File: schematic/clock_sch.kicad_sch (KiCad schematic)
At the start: 3 parts

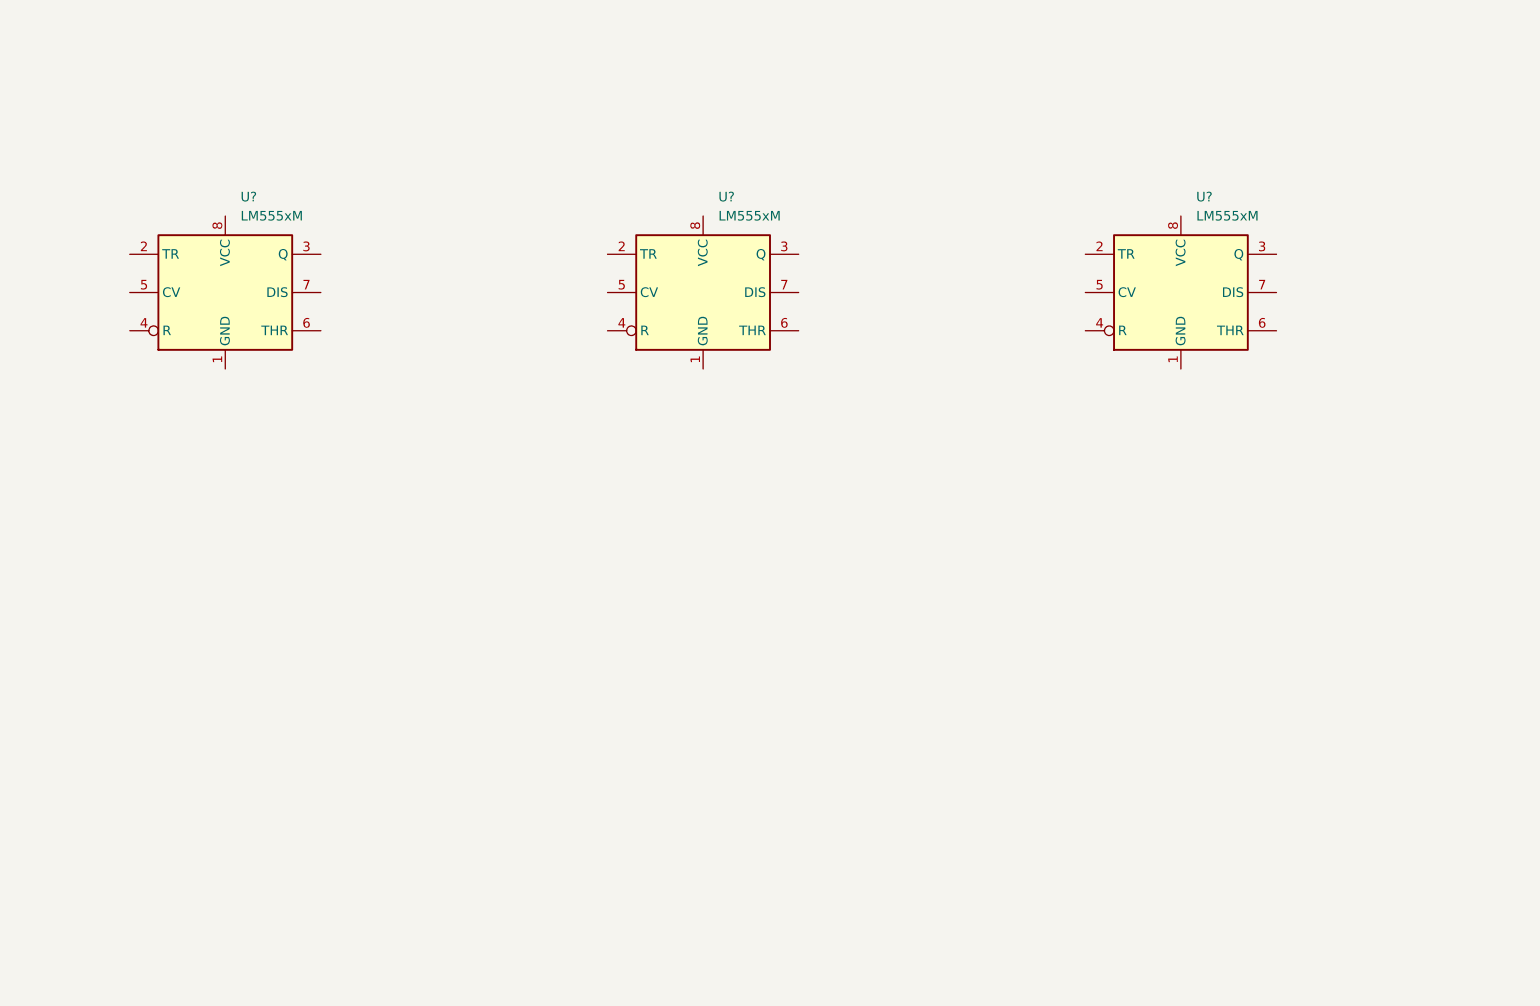
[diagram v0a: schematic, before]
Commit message: added astable clock schematic
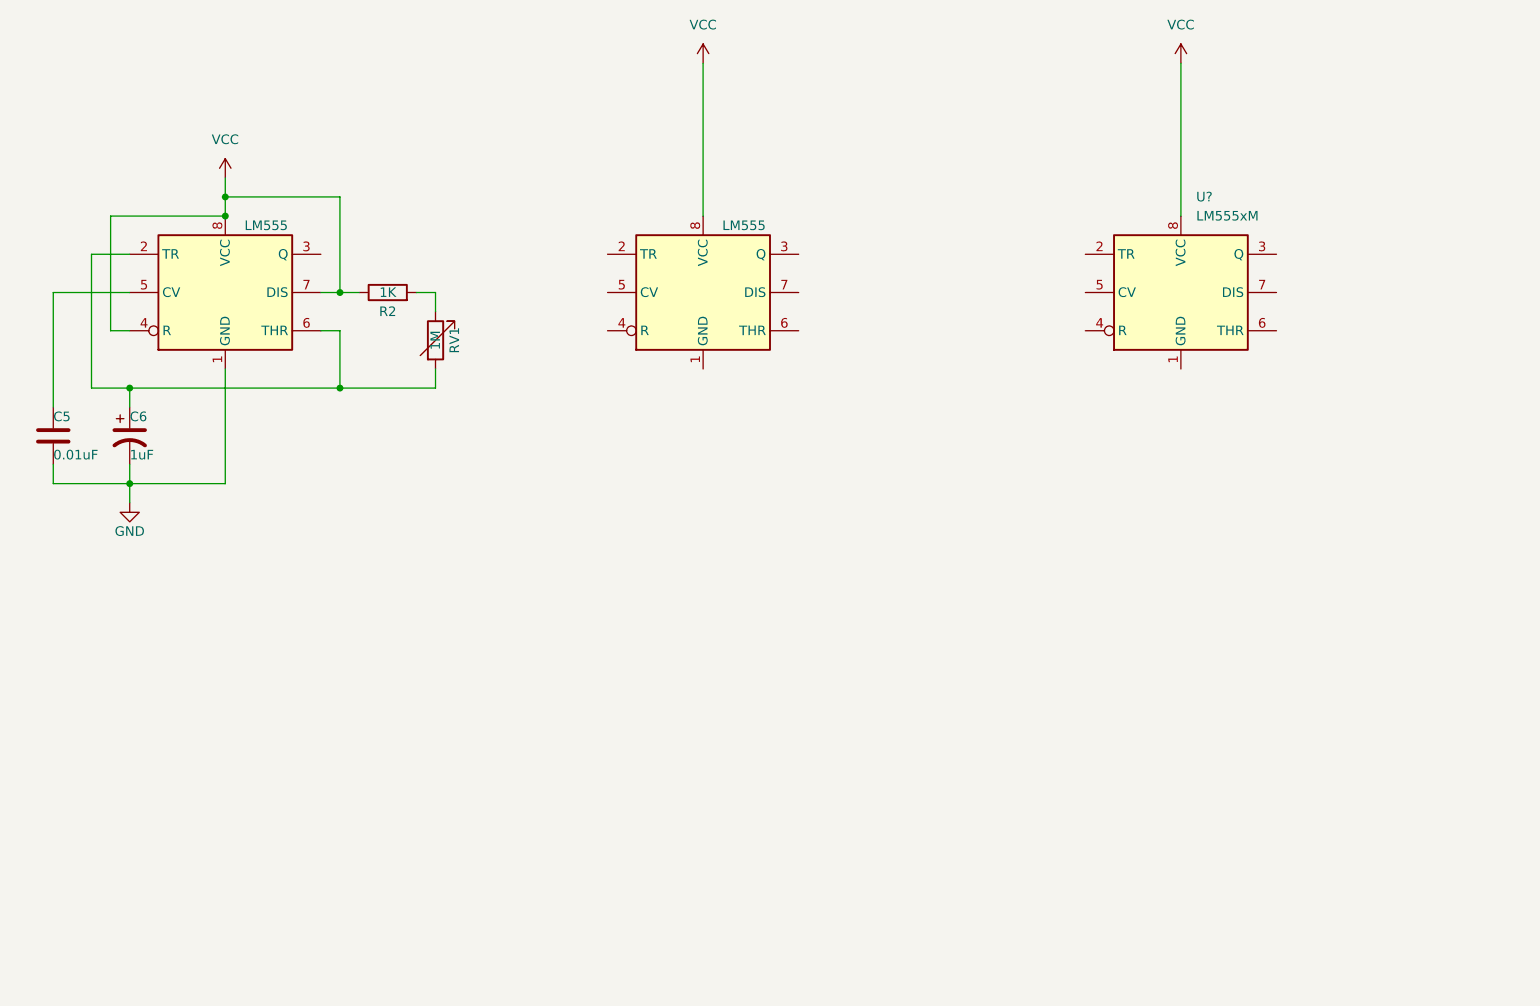
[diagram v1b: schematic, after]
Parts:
- added C5: 0.01uF, symbol Device:C
- added C6: 1uF, symbol Device:C_Polarized_US
- added R2: 1K, symbol Device:R
- added RV1: 1M, symbol Device:R_Variable
- U? (x2): value LM555xM -> LM555
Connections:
- net VCC: now reaches U?.8 (VCC)
- net VCC: now also U?.4 (R), U?.7 (DIS), U?.8 (VCC), U?.8 (VCC), R2.1
- net GND: now reaches U?.1 (GND)
- net GND: now also C5.2, C6.2
- net at U?.2 (TR): now also U?.6 (THR), C6.1, RV1.2
- net at U?.5 (CV): now also C5.1
- new net: R2.2, RV1.1
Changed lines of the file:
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@@
 (kicad_sch (version 20211123) (generator eeschema)
   (paper "A4")
+  (junction (at 63.5 60.96) (diameter 0) (color 0 0 0 0)
+  )
+  (junction (at 78.74 71.12) (diameter 0) (color 0 0 0 0)
+  )
+  (junction (at 63.5 58.42) (diameter 0) (color 0 0 0 0)
+  )
+  (junction (at 50.8 83.82) (diameter 0) (color 0 0 0 0)
+  )
+  (junction (at 78.74 83.82) (diameter 0) (color 0 0 0 0)
+  )
+  (junction (at 50.8 96.52) (diameter 0) (color 0 0 0 0)
+  )
+  (wire (pts (xy 63.5 60.96) (xy 48.26 60.96))
+    (stroke (width 0) (type default) (color 0 0 0 0))
+  )
+  (wire (pts (xy 63.5 55.88) (xy 63.5 58.42))
+    (stroke (width 0) (type default) (color 0 0 0 0))
+  )
+  (wire (pts (xy 91.44 81.28) (xy 91.44 83.82))
+    (stroke (width 0) (type default) (color 0 0 0 0))
+  )
+  (wire (pts (xy 190.5 40.64) (xy 190.5 60.96))
+    (stroke (width 0) (type default) (color 0 0 0 0))
+  )
+  (wire (pts (xy 78.74 58.42) (xy 78.74 71.12))
+    (stroke (width 0) (type default) (color 0 0 0 0))
+  )
+  (wire (pts (xy 78.74 83.82) (xy 91.44 83.82))
+    (stroke (width 0) (type default) (color 0 0 0 0))
+  )
+  (wire (pts (xy 76.2 76.2) (xy 78.74 76.2))
+    (stroke (width 0) (type default) (color 0 0 0 0))
+  )
+  (wire (pts (xy 78.74 71.12) (xy 81.28 71.12))
+    (stroke (width 0) (type default) (color 0 0 0 0))
+  )
+  (wire (pts (xy 50.8 93.98) (xy 50.8 96.52))
+    (stroke (width 0) (type default) (color 0 0 0 0))
+  )
+  (wire (pts (xy 40.64 71.12) (xy 40.64 86.36))
+    (stroke (width 0) (type default) (color 0 0 0 0))
+  )
+  (wire (pts (xy 63.5 58.42) (xy 63.5 60.96))
+    (stroke (width 0) (type default) (color 0 0 0 0))
+  )
+  (wire (pts (xy 48.26 60.96) (xy 48.26 76.2))
+    (stroke (width 0) (type default) (color 0 0 0 0))
+  )
+  (wire (pts (xy 50.8 71.12) (xy 40.64 71.12))
+    (stroke (width 0) (type default) (color 0 0 0 0))
+  )
+  (wire (pts (xy 50.8 83.82) (xy 78.74 83.82))
+    (stroke (width 0) (type default) (color 0 0 0 0))
+  )
+  (wire (pts (xy 91.44 71.12) (xy 91.44 73.66))
+    (stroke (width 0) (type default) (color 0 0 0 0))
+  )
+  (wire (pts (xy 63.5 58.42) (xy 78.74 58.42))
+    (stroke (width 0) (type default) (color 0 0 0 0))
+  )
+  (wire (pts (xy 127 40.64) (xy 127 60.96))
+    (stroke (width 0) (type default) (color 0 0 0 0))
+  )
+  (wire (pts (xy 88.9 71.12) (xy 91.44 71.12))
+    (stroke (width 0) (type default) (color 0 0 0 0))
+  )
+  (wire (pts (xy 45.72 83.82) (xy 45.72 66.04))
+    (stroke (width 0) (type default) (color 0 0 0 0))
+  )
+  (wire (pts (xy 40.64 93.98) (xy 40.64 96.52))
+    (stroke (width 0) (type default) (color 0 0 0 0))
+  )
+  (wire (pts (xy 50.8 83.82) (xy 50.8 86.36))
+    (stroke (width 0) (type default) (color 0 0 0 0))
+  )
+  (wire (pts (xy 76.2 71.12) (xy 78.74 71.12))
+    (stroke (width 0) (type default) (color 0 0 0 0))
+  )
+  (wire (pts (xy 45.72 66.04) (xy 50.8 66.04))
+    (stroke (width 0) (type default) (color 0 0 0 0))
+  )
+  (wire (pts (xy 48.26 76.2) (xy 50.8 76.2))
+    (stroke (width 0) (type default) (color 0 0 0 0))
+  )
+  (wire (pts (xy 45.72 83.82) (xy 50.8 83.82))
+    (stroke (width 0) (type default) (color 0 0 0 0))
+  )
+  (wire (pts (xy 78.74 76.2) (xy 78.74 83.82))
+    (stroke (width 0) (type default) (color 0 0 0 0))
+  )
+  (wire (pts (xy 50.8 96.52) (xy 50.8 99.06))
+    (stroke (width 0) (type default) (color 0 0 0 0))
+  )
+  (wire (pts (xy 50.8 96.52) (xy 63.5 96.52))
+    (stroke (width 0) (type default) (color 0 0 0 0))
+  )
+  (wire (pts (xy 63.5 81.28) (xy 63.5 96.52))
+    (stroke (width 0) (type default) (color 0 0 0 0))
+  )
+  (wire (pts (xy 40.64 96.52) (xy 50.8 96.52))
+    (stroke (width 0) (type default) (color 0 0 0 0))
+  )
   (symbol (lib_id "Timer:LM555xM") (at 127 71.12 0) (unit 1)
-    (in_bom yes) (on_board yes) (fields_autoplaced)
+    (in_bom yes) (on_board yes)
     (property "Reference" "U?" (id 0) (at 129.0194 58.42 0)
-      (effects (font (size 1.27 1.27)) (justify left))
-    )
-    (property "Value" "LM555xM" (id 1) (at 129.0194 60.96 0)
+      (effects (font (size 1.27 1.27)) (justify left) hide)
+    )
+    (property "Value" "LM555" (id 1) (at 129.54 62.23 0)
       (effects (font (size 1.27 1.27)) (justify left))
     )
@@
   )
   (symbol (lib_id "Timer:LM555xM") (at 63.5 71.12 0) (unit 1)
-    (in_bom yes) (on_board yes) (fields_autoplaced)
+    (in_bom yes) (on_board yes)
     (property "Reference" "U?" (id 0) (at 65.5194 58.42 0)
-      (effects (font (size 1.27 1.27)) (justify left))
-    )
-    (property "Value" "LM555xM" (id 1) (at 65.5194 60.96 0)
+      (effects (font (size 1.27 1.27)) (justify left) hide)
+    )
+    (property "Value" "LM555" (id 1) (at 66.04 62.23 0)
       (effects (font (size 1.27 1.27)) (justify left))
     )
@@
     (pin "7")
   )
+  (symbol (lib_id "power:VCC") (at 190.5 40.64 0) (unit 1)
+    (in_bom yes) (on_board yes) (fields_autoplaced)
+    (property "Reference" "#PWR?" (id 0) (at 190.5 44.45 0)
+      (effects (font (size 1.27 1.27)) hide)
+    )
+    (property "Value" "VCC" (id 1) (at 190.5 35.56 0))
+    (property "Footprint" "" (id 2) (at 190.5 40.64 0)
+      (effects (font (size 1.27 1.27)) hide)
+    )
+    (property "Datasheet" "" (id 3) (at 190.5 40.64 0)
+      (effects (font (size 1.27 1.27)) hide)
+    )
+    (pin "1")
+  )
+  (symbol (lib_id "power:VCC") (at 127 40.64 0) (unit 1)
+    (in_bom yes) (on_board yes) (fields_autoplaced)
+    (property "Reference" "#PWR?" (id 0) (at 127 44.45 0)
+      (effects (font (size 1.27 1.27)) hide)
+    )
+    (property "Value" "VCC" (id 1) (at 127 35.56 0))
+    (property "Footprint" "" (id 2) (at 127 40.64 0)
+      (effects (font (size 1.27 1.27)) hide)
+    )
+    (property "Datasheet" "" (id 3) (at 127 40.64 0)
+      (effects (font (size 1.27 1.27)) hide)
+    )
+    (pin "1")
+  )
+  (symbol (lib_id "Device:R_Variable") (at 91.44 77.47 0) (unit 1)
+    (in_bom yes) (on_board yes)
+    (property "Reference" "RV1" (id 0) (at 93.98 77.47 90))
+    (property "Value" "1M" (id 1) (at 91.44 77.47 90))
+    (property "Footprint" "" (id 2) (at 89.662 77.47 90)
+      (effects (font (size 1.27 1.27)) hide)
+    )
+    (property "Datasheet" "~" (id 3) (at 91.44 77.47 0)
+      (effects (font (size 1.27 1.27)) hide)
+    )
+    (pin "1")
+    (pin "2")
+  )
+  (symbol (lib_id "Device:C") (at 40.64 90.17 0) (unit 1)
+    (in_bom yes) (on_board yes)
+    (property "Reference" "C5" (id 0) (at 40.64 87.63 0)
+      (effects (font (size 1.27 1.27)) (justify left))
+    )
+    (property "Value" "0.01uF" (id 1) (at 40.64 92.71 0)
+      (effects (font (size 1.27 1.27)) (justify left))
+    )
+    (property "Footprint" "" (id 2) (at 41.6052 93.98 0)
+      (effects (font (size 1.27 1.27)) hide)
+    )
+    (property "Datasheet" "~" (id 3) (at 40.64 90.17 0)
+      (effects (font (size 1.27 1.27)) hide)
+    )
+    (pin "1")
+    (pin "2")
+  )
+  (symbol (lib_id "power:VCC") (at 63.5 55.88 0) (unit 1)
+    (in_bom yes) (on_board yes) (fields_autoplaced)
+    (property "Reference" "#PWR?" (id 0) (at 63.5 59.69 0)
+      (effects (font (size 1.27 1.27)) hide)
+    )
+    (property "Value" "VCC" (id 1) (at 63.5 50.8 0))
+    (property "Footprint" "" (id 2) (at 63.5 55.88 0)
+      (effects (font (size 1.27 1.27)) hide)
+    )
+    (property "Datasheet" "" (id 3) (at 63.5 55.88 0)
+      (effects (font (size 1.27 1.27)) hide)
+    )
+    (pin "1")
+  )
+  (symbol (lib_id "Device:C_Polarized_US") (at 50.8 90.17 0) (unit 1)
+    (in_bom yes) (on_board yes)
+    (property "Reference" "C6" (id 0) (at 50.8 87.63 0)
+      (effects (font (size 1.27 1.27)) (justify left))
+    )
+    (property "Value" "1uF" (id 1) (at 50.8 92.71 0)
+      (effects (font (size 1.27 1.27)) (justify left))
+    )
+    (property "Footprint" "" (id 2) (at 50.8 90.17 0)
+      (effects (font (size 1.27 1.27)) hide)
+    )
+    (property "Datasheet" "~" (id 3) (at 50.8 90.17 0)
+      (effects (font (size 1.27 1.27)) hide)
+    )
+    (pin "1")
+    (pin "2")
+  )
+  (symbol (lib_id "Device:R") (at 85.09 71.12 90) (unit 1)
+    (in_bom yes) (on_board yes)
+    (property "Reference" "R2" (id 0) (at 85.09 73.66 90))
+    (property "Value" "1K" (id 1) (at 85.09 71.12 90))
+    (property "Footprint" "" (id 2) (at 85.09 72.898 90)
+      (effects (font (size 1.27 1.27)) hide)
+    )
+    (property "Datasheet" "~" (id 3) (at 85.09 71.12 0)
+      (effects (font (size 1.27 1.27)) hide)
+    )
+    (pin "1")
+    (pin "2")
+  )
+  (symbol (lib_id "power:GND") (at 50.8 99.06 0) (unit 1)
+    (in_bom yes) (on_board yes)
+    (property "Reference" "#PWR?" (id 0) (at 50.8 105.41 0)
+      (effects (font (size 1.27 1.27)) hide)
+    )
+    (property "Value" "GND" (id 1) (at 50.8 102.87 0))
+    (property "Footprint" "" (id 2) (at 50.8 99.06 0)
+      (effects (font (size 1.27 1.27)) hide)
+    )
+    (property "Datasheet" "" (id 3) (at 50.8 99.06 0)
+      (effects (font (size 1.27 1.27)) hide)
+    )
+    (pin "1")
+  )
 )
